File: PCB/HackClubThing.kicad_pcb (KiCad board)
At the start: 2 copper layers, 75 x 65 mm, 13 parts, among them SW1 SW_Push, SW2 SW_Push, SW3 SW_Push, SW4 SW_Push, SW5 SW_Push, SW6 RotaryEncoder_Switch, U1 MOUDLE-SEEEDUINO-XIAO, U2 ER_OLEDM0.91_1x-I2C

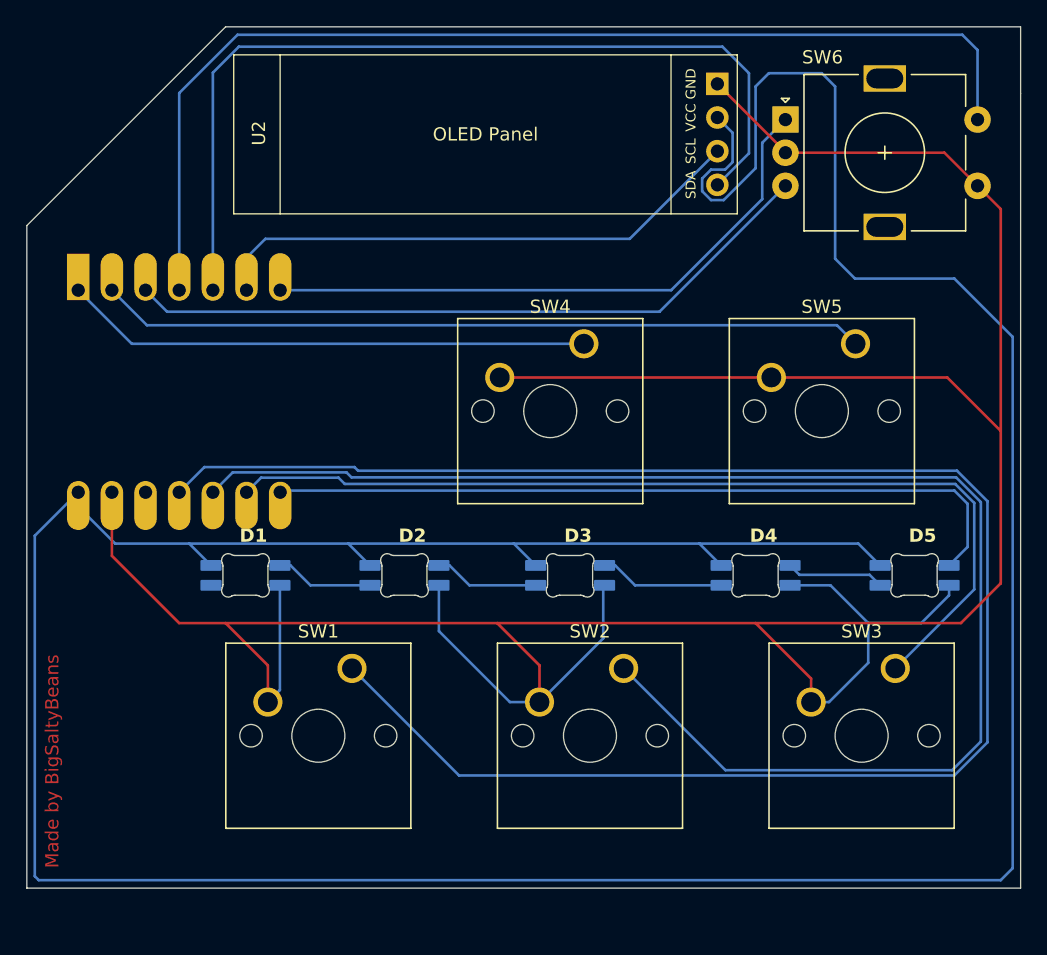
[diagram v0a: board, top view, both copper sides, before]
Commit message: Moved Key and LED Locations and added backlighting
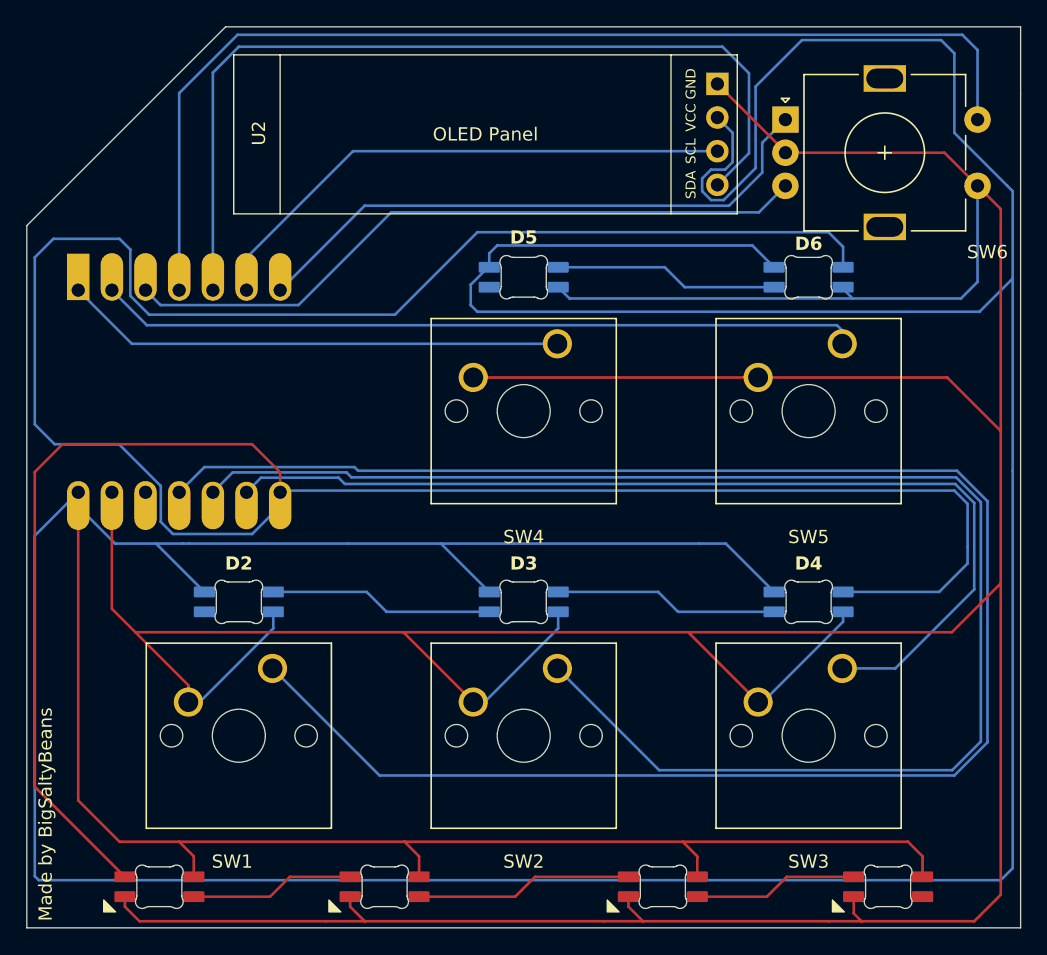
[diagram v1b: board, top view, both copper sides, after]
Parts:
- added D6: SK6812MINI-E, HackClubCarePackage:SK6812MINI-E_fixed, F.Cu at (174.0, 99.0)
- added D7: SK6812MINI-E, HackClubCarePackage:SK6812MINI-E_fixed, B.Cu at (163.0, 145.0)
- added D8: SK6812MINI-E, HackClubCarePackage:SK6812MINI-E_fixed, B.Cu at (142.0, 145.0)
- added D9: SK6812MINI-E, HackClubCarePackage:SK6812MINI-E_fixed, B.Cu at (125.0, 145.0)
- D1: moved to B.Cu
- moved D1 53.9 mm to (180.0, 145.0), turned to 180 degrees
- moved D5 37.1 mm to (152.5, 99.0)
- moved D2 12.7 mm to (131.0, 123.5)
- moved SW1 6.00 mm to (133.5, 128.4)
- moved SW2 5.00 mm to (155.0, 128.4)
- moved D4 4.47 mm to (174.0, 123.5)
- moved D3 4.03 mm to (152.5, 123.5)
- moved SW3 4.00 mm to (176.5, 128.4)
- moved SW4 2.00 mm to (155.0, 103.9)
- moved SW5 1.00 mm to (176.5, 103.9)
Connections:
- D2 pad 2: Net-(D1-DIN) -> unconnected-(D2-DOUT-Pad2)
- D5 pad 2: Net-(D4-DIN) -> unconnected-(D5-DOUT-Pad2)
- U1 pad 8: Net-(D5-DIN) -> Net-(D4-DIN)
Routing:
- net Net-(D4-DIN): track 7.42 -> 230.9 mm
- net Net-(D1-VDD): track 272.2 -> 439.2 mm
- net GND: track 252.2 -> 368.8 mm
- net Net-(D5-DIN): track 57.6 -> 16.9 mm
- net Net-(D7-DIN): track 0.00 -> 16.4 mm
- net Net-(D8-DIN): track 0.00 -> 12.4 mm
- net Net-(D2-DIN): track 7.92 -> 16.9 mm
- net Net-(D3-DIN): track 9.42 -> 16.9 mm
- net Net-(U1-PA6_A10_D10_MOSI): track 133.4 -> 139.4 mm
- net Net-(D1-DIN): track 7.42 -> 12.4 mm
- net Net-(U1-PA5_A9_D9_MISO): track 108.6 -> 113.6 mm
- net Net-(U1-PA7_A8_D8_SCK): track 71.1 -> 75.1 mm
- net Net-(U1-PA02_A0_D0): track 39.8 -> 37.8 mm
- net Net-(U1-PB08_A6_D6_TX): track 47.9 -> 46.7 mm
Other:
- board size 75 x 65 mm -> 75 x 68 mm
